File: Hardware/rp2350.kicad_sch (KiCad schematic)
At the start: 40 parts, among them J1 Conn_01x03, J5 USB_C_Receptacle, SW1 SMD_4.6x2.8mm_h2.5mm, SW2 SMD_4.6x2.8mm_h2.5mm, SW4 SMD_4.6x2.8mm_h2.5mm, U4 W25Q128JVPIM

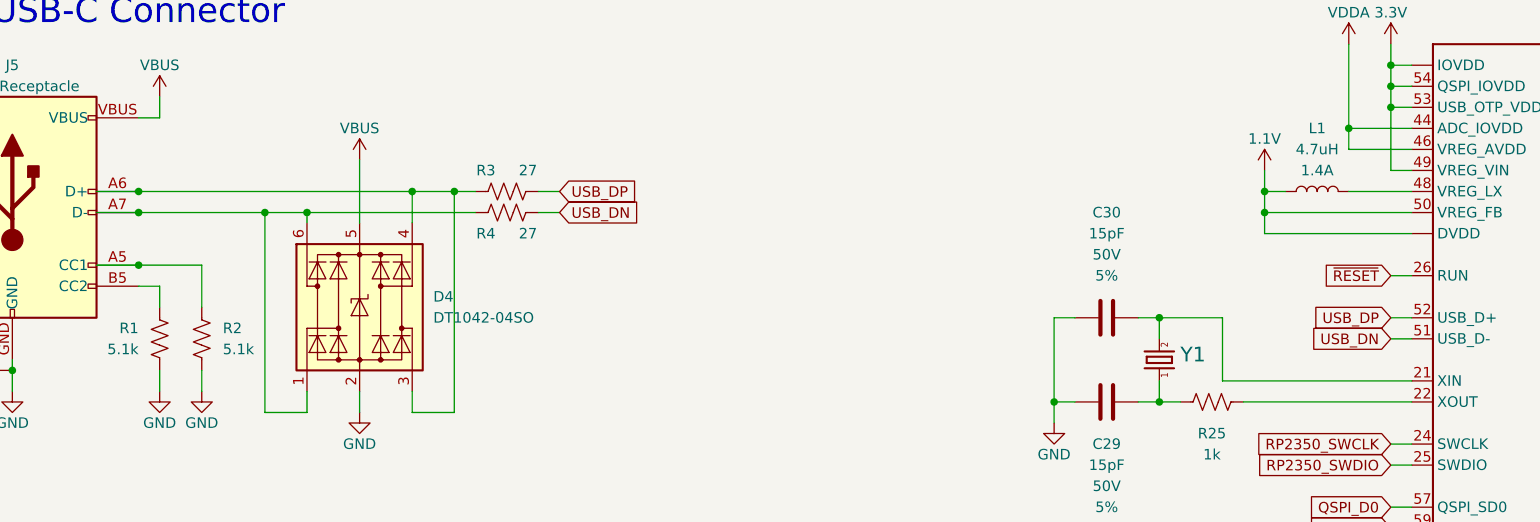
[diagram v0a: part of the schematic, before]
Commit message: Initial board layout
Board outline determined based off selected enclosure
Clusters of components placed and routed
Waiting for feedback before finishing routing
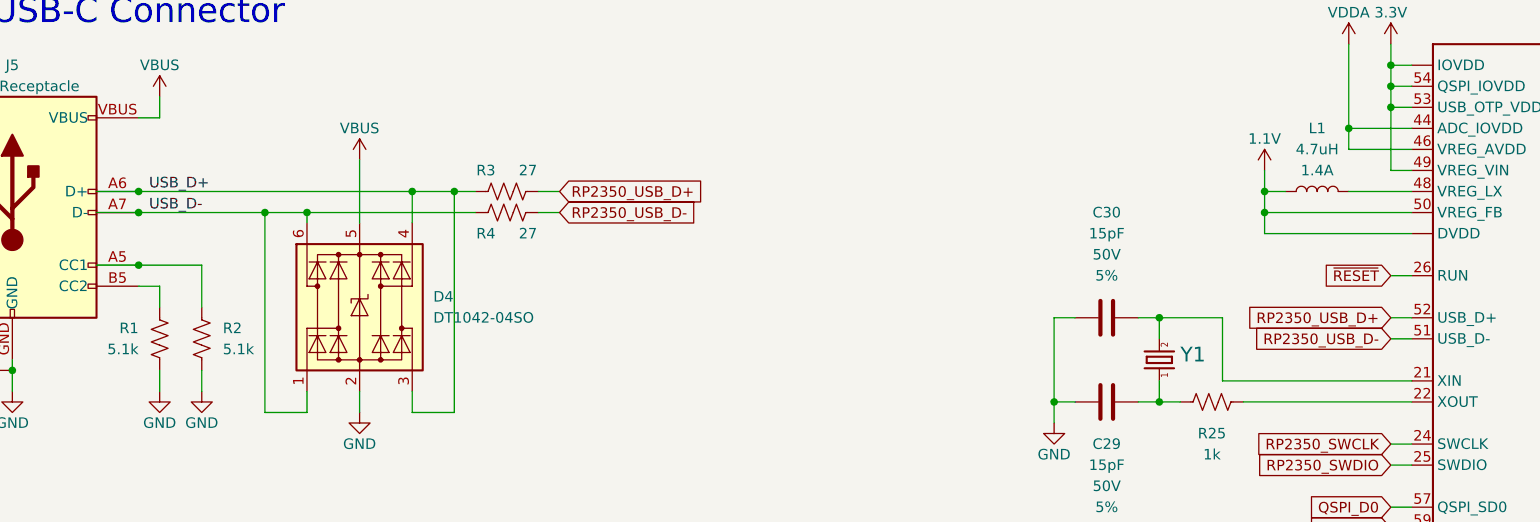
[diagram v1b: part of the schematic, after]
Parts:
- removed SW4: SMD_4.6x2.8mm_h2.5mm, SparkFun-Switch:Push_SMD_4.6x2.8mm, symbol SparkFun-Switch:SPST_Push_SMD_4.6x2.8mm_h2.5mm
- added SW4: PTH_RA_h7.5mm, SparkFun-Switch:Push_PTH_RA_8-020_h7.5mm, symbol SparkFun-Switch:SPST_Push_PTH_RA_h7.5mm
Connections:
- net GND: now also SW4.1
- net USER_BUTTON: now also SW4.2
- net USB_D-: now reaches D4.1 (I/O1), D4.6 (I/O4), J5.A7 (D-), J5.B7 (D-), R4.2
- net USB_D+: now reaches D4.3 (I/O2), D4.4 (I/O3), J5.A6 (D+), J5.B6 (D+), R3.2
- net USB_DN renamed RP2350_USB_D-
- net USB_DP renamed RP2350_USB_D+
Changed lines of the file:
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@@
 		)
 	)
+	(label "USB_D+"
+		(at 58.42 45.72 0)
+		(fields_autoplaced yes)
+		(effects
+			(font
+				(size 1.27 1.27)
+			)
+			(justify left bottom)
+		)
+	)
+	(label "USB_D-"
+		(at 58.42 48.26 0)
+		(fields_autoplaced yes)
+		(effects
+			(font
+				(size 1.27 1.27)
+			)
+			(justify left bottom)
+		)
+	)
 	(global_label "~{BOOT}"
 		(shape input)
@@
 		)
 	)
-	(global_label "USB_DN"
+	(global_label "RP2350_USB_D-"
 		(shape input)
 		(at 107.95 48.26 0)
@@
 		)
 		(property "Intersheetrefs" "${INTERSHEET_REFS}"
-			(at 118.3133 48.26 0)
+			(at 126.9008 48.26 0)
 			(effects
 				(font
@@
 		)
 	)
-	(global_label "USB_DN"
+	(global_label "RP2350_USB_D-"
 		(shape input)
 		(at 208.28 63.5 180)
@@
 		)
 		(property "Intersheetrefs" "${INTERSHEET_REFS}"
-			(at 197.9167 63.5 0)
+			(at 189.3292 63.5 0)
 			(effects
 				(font
@@
 		)
 	)
-	(global_label "USB_DP"
+	(global_label "RP2350_USB_D+"
 		(shape input)
 		(at 208.28 60.96 180)
@@
 		)
 		(property "Intersheetrefs" "${INTERSHEET_REFS}"
-			(at 197.9772 60.96 0)
+			(at 189.3292 60.96 0)
 			(effects
 				(font
@@
 		)
 	)
-	(global_label "USB_DP"
+	(global_label "RP2350_USB_D+"
 		(shape input)
 		(at 107.95 45.72 0)
@@
 		)
 		(property "Intersheetrefs" "${INTERSHEET_REFS}"
-			(at 118.2528 45.72 0)
+			(at 126.9008 45.72 0)
 			(effects
 				(font
@@
 	)
 	(symbol
-		(lib_id "SparkFun-Switch:SPST_Push_SMD_4.6x2.8mm_h2.5mm")
-		(at 35.56 137.16 90)
-		(unit 1)
-		(exclude_from_sim no)
-		(in_bom yes)
-		(on_board yes)
-		(dnp no)
-		(fields_autoplaced yes)
-		(property "Reference" "SW4"
-			(at 36.83 137.1599 90)
-			(effects
-				(font
-					(size 1.27 1.27)
-				)
-				(justify right)
-			)
-		)
-		(property "Value" "SMD_4.6x2.8mm_h2.5mm"
-			(at 36.83 138.4299 90)
-			(effects
-				(font
-					(size 1.27 1.27)
-				)
-				(justify right)
-				(hide yes)
-			)
-		)
-		(property "Footprint" "SparkFun-Switch:Push_SMD_4.6x2.8mm"
-			(at 40.64 137.16 0)
-			(effects
-				(font
-					(size 1.27 1.27)
-				)
-				(hide yes)
-			)
-		)
-		(property "Datasheet" "~"
-			(at 45.72 137.16 0)
-			(effects
-				(font
-					(size 1.27 1.27)
-				)
-				(hide yes)
-			)
-		)
-		(property "Description" "Single Pole Single Throw (SPST) switch"
-			(at 35.56 137.16 0)
-			(effects
-				(font
-					(size 1.27 1.27)
-				)
-				(hide yes)
-			)
-		)
-		(property "PROD_ID" "SWCH-15606"
-			(at 43.18 137.16 0)
-			(effects
-				(font
-					(size 1.27 1.27)
-				)
-				(hide yes)
-			)
-		)
-		(pin "2"
-		)
-		(pin "1"
-		)
-		(instances
-			(project "SparkFun_IoT_Node_LoRaWAN"
-				(path "/e3dd3ae4-244d-4cba-9cca-5d2abf83f29a/590da06b-12fb-4a03-9ce6-308c286b4365"
-					(reference "SW4")
-					(unit 1)
-				)
-			)
-		)
-	)
-	(symbol
 		(lib_id "RP2350A:RP2350A")
 		(at 228.6 68.58 0)
@@
 					(unit 1)
 				)
+			)
+		)
+	)
+	(symbol
+		(lib_id "SparkFun-Switch:SPST_Push_PTH_RA_h7.5mm")
+		(at 35.56 137.16 90)
+		(unit 1)
+		(exclude_from_sim no)
+		(in_bom yes)
+		(on_board yes)
+		(dnp no)
+		(fields_autoplaced yes)
+		(property "Reference" "SW4"
+			(at 36.83 137.1599 90)
+			(effects
+				(font
+					(size 1.27 1.27)
+				)
+				(justify right)
+			)
+		)
+		(property "Value" "PTH_RA_h7.5mm"
+			(at 36.83 138.4299 90)
+			(effects
+				(font
+					(size 1.27 1.27)
+				)
+				(justify right)
+				(hide yes)
+			)
+		)
+		(property "Footprint" "SparkFun-Switch:Push_PTH_RA_8-020_h7.5mm"
+			(at 40.64 137.16 0)
+			(effects
+				(font
+					(size 1.27 1.27)
+				)
+				(hide yes)
+			)
+		)
+		(property "Datasheet" "~"
+			(at 45.72 137.16 0)
+			(effects
+				(font
+					(size 1.27 1.27)
+				)
+				(hide yes)
+			)
+		)
+		(property "Description" "Single Pole Single Throw (SPST) switch"
+			(at 35.56 137.16 0)
+			(effects
+				(font
+					(size 1.27 1.27)
+				)
+				(hide yes)
+			)
+		)
+		(property "PROD_ID" "SWCH-13896"
+			(at 43.18 137.16 0)
+			(effects
+				(font
+					(size 1.27 1.27)
+				)
+				(hide yes)
+			)
+		)
+		(property "Mfg Part#" "8-020 TS H = 7.5mm"
+			(at 48.26 137.16 0)
+			(effects
+				(font
+					(size 1.27 1.27)
+				)
+				(hide yes)
+			)
+		)
+		(pin "M2"
+		)
+		(pin "1"
+		)
+		(pin "M1"
+		)
+		(pin "2"
+		)
+		(instances
+			(project ""
+				(path "/e3dd3ae4-244d-4cba-9cca-5d2abf83f29a/590da06b-12fb-4a03-9ce6-308c286b4365"
+					(reference "SW4")
+					(unit 1)
+				)

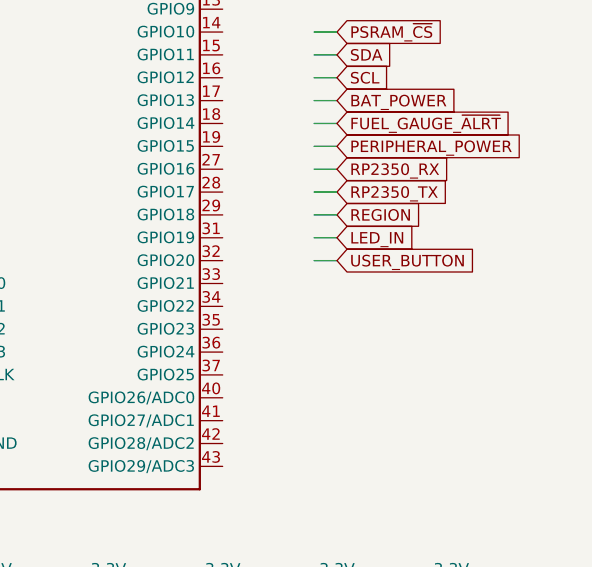
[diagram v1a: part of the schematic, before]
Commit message: Review updates
Remove region selection resistors
Add uSD card connector
Move XBLR USB connector within enclosure
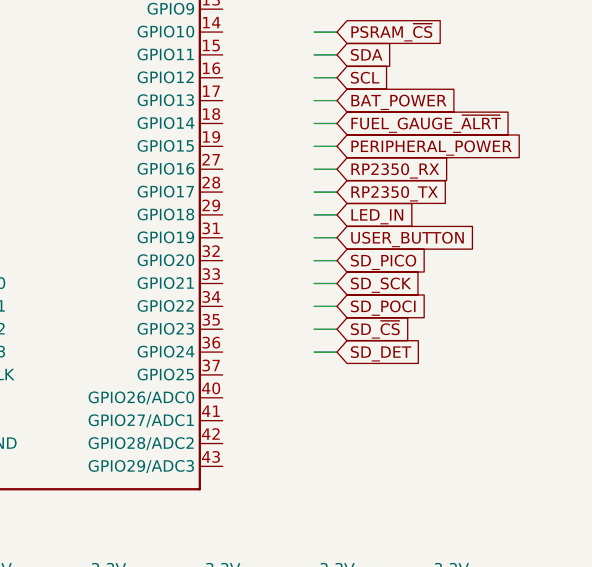
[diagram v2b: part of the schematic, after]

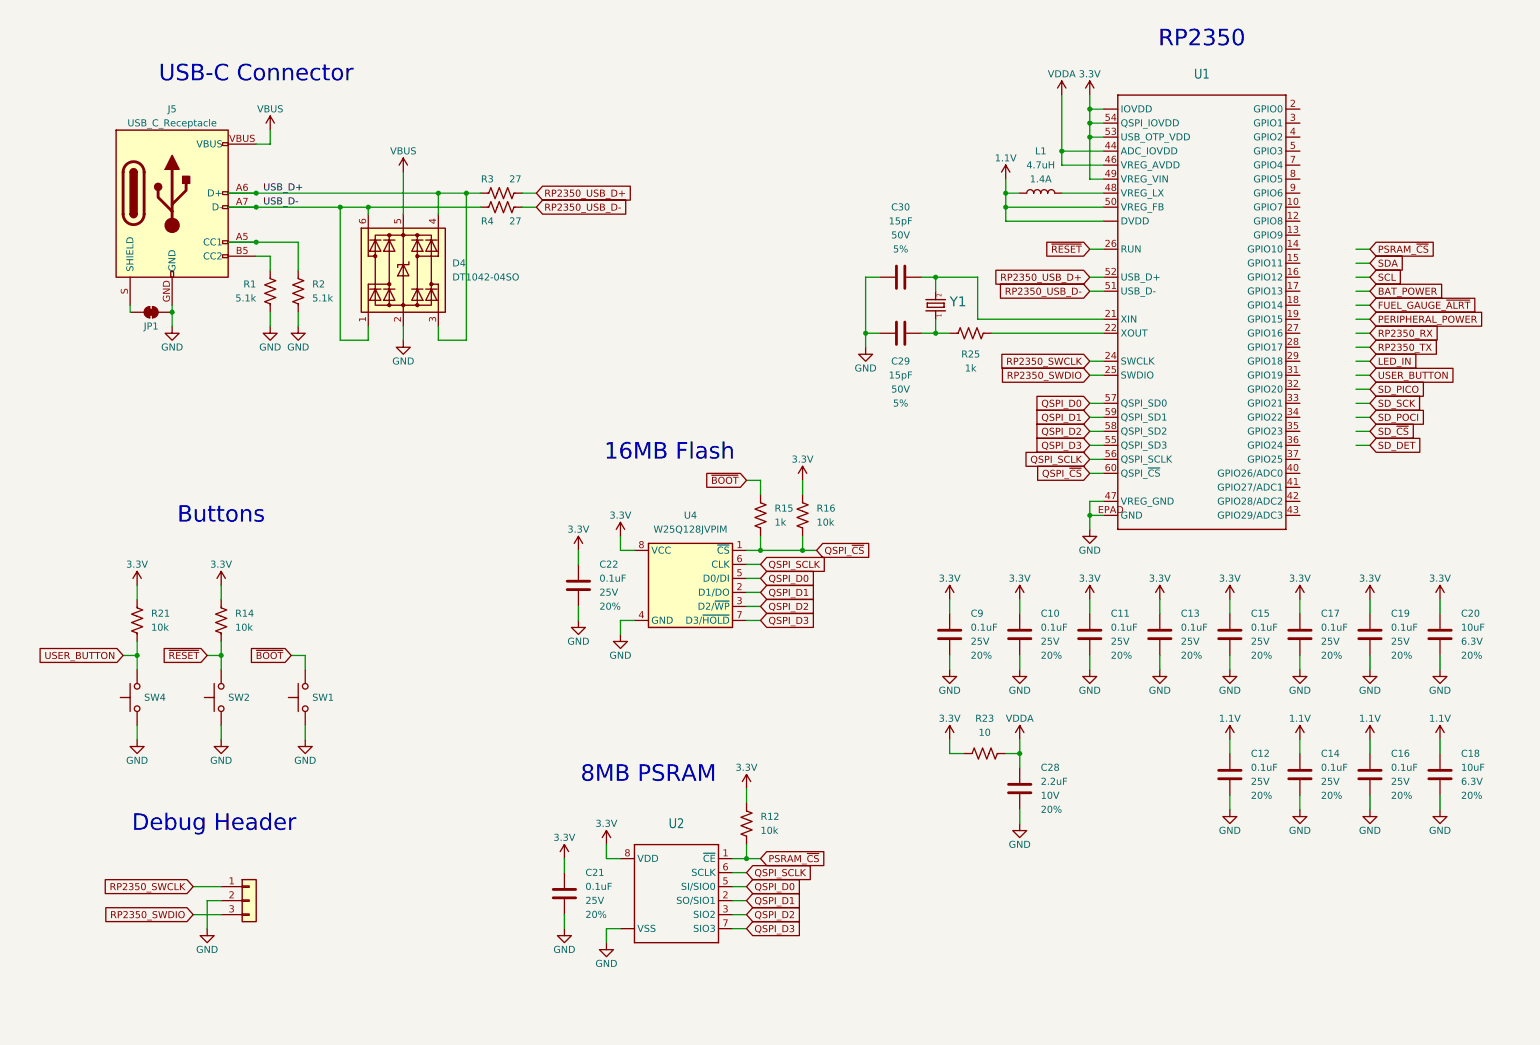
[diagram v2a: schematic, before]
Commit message: Finish connections and routing
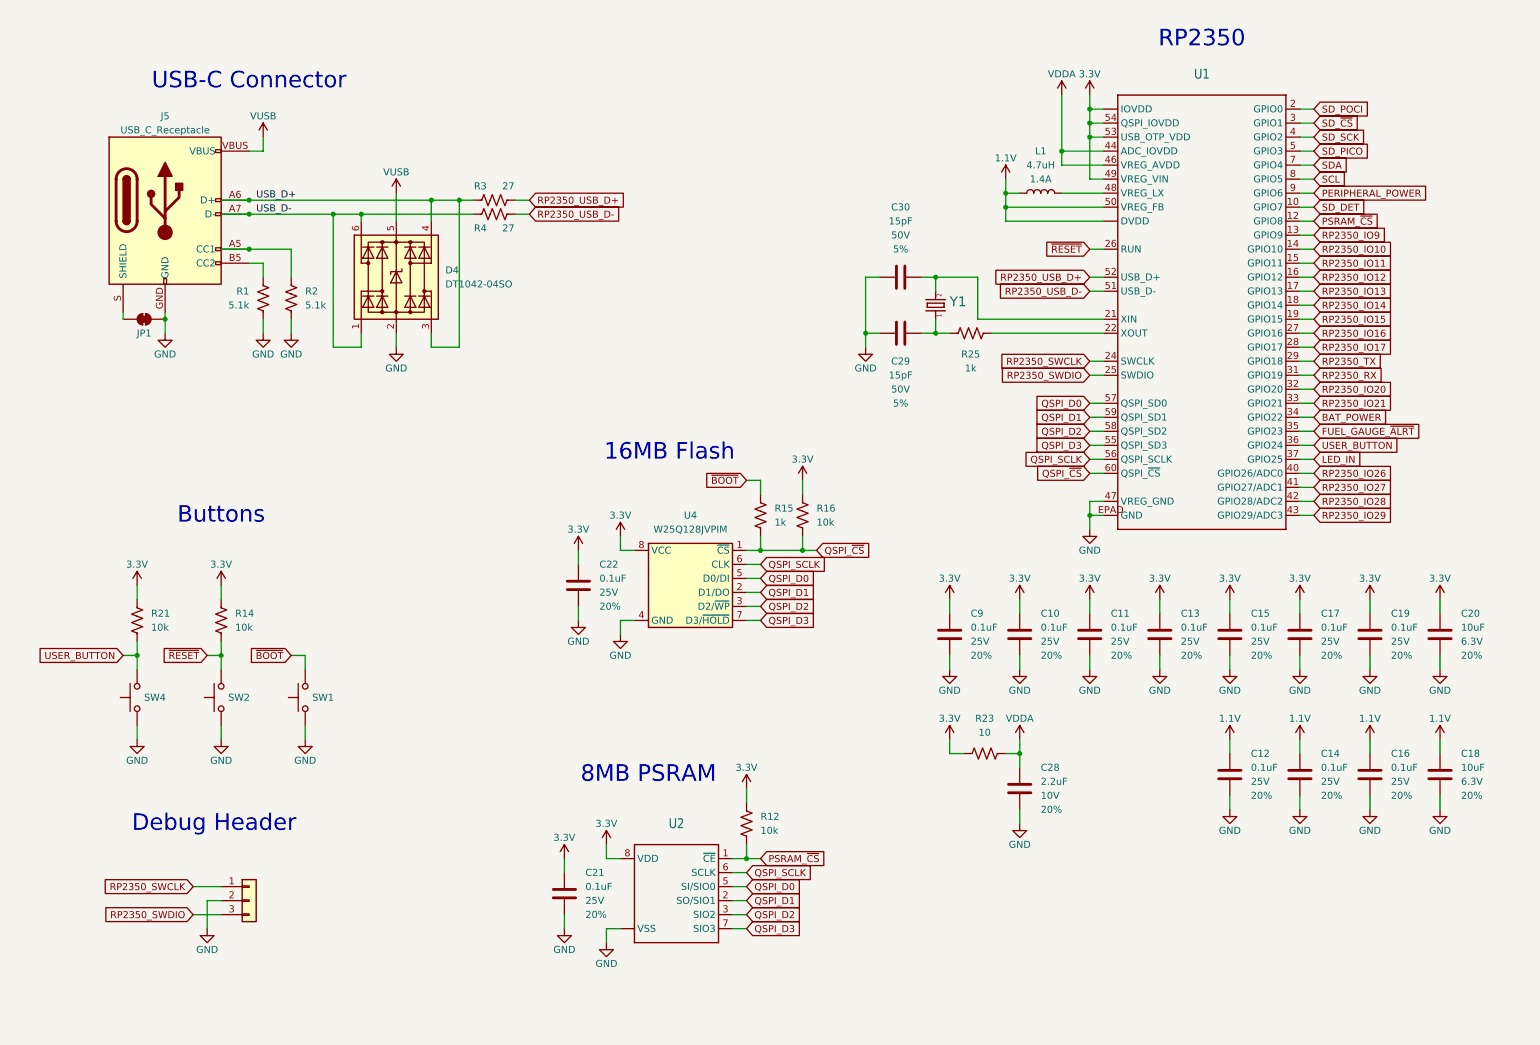
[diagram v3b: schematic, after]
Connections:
- net BAT_POWER: now also U1.34 (GPIO22)
- net FUEL_GAUGE_~{ALRT}: now also U1.35 (GPIO23)
- net LED_IN: now also U1.37 (GPIO25)
- net PERIPHERAL_POWER: now also U1.9 (GPIO6)
- net PSRAM_~{CS}: now also U1.12 (GPIO8)
- net RP2350_RX: now also U1.31 (GPIO19)
- net RP2350_TX: now also U1.29 (GPIO18)
- net SCL: now also U1.8 (GPIO5)
- net SDA: now also U1.7 (GPIO4)
- net SD_DET: now also U1.10 (GPIO7)
- net SD_PICO: now also U1.5 (GPIO3)
- net SD_POCI: now also U1.2 (GPIO0)
- net SD_SCK: now also U1.4 (GPIO2)
- net SD_~{CS}: now also U1.3 (GPIO1)
- net USER_BUTTON: now also U1.36 (GPIO24)
- net RP2350_IO9: now reaches U1.13 (GPIO9)
- net RP2350_IO10: now reaches U1.14 (GPIO10)
- net RP2350_IO11: now reaches U1.15 (GPIO11)
- net RP2350_IO12: now reaches U1.16 (GPIO12)
- net RP2350_IO13: now reaches U1.17 (GPIO13)
- net RP2350_IO14: now reaches U1.18 (GPIO14)
- net RP2350_IO15: now reaches U1.19 (GPIO15)
- net RP2350_IO16: now reaches U1.27 (GPIO16)
- net RP2350_IO17: now reaches U1.28 (GPIO17)
- net RP2350_IO20: now reaches U1.32 (GPIO20)
- net RP2350_IO21: now reaches U1.33 (GPIO21)
- net RP2350_IO26: now reaches U1.40 (GPIO26/ADC0)
- net RP2350_IO27: now reaches U1.41 (GPIO27/ADC1)
- net RP2350_IO28: now reaches U1.42 (GPIO28/ADC2)
- net RP2350_IO29: now reaches U1.43 (GPIO29/ADC3)
- net VBUS renamed VUSB
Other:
- moved on the sheet: D4, J5, JP1, R1, R2, R3, R4

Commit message: Clean up schematic
Add lines between regions
Add instruction text to all jumpers
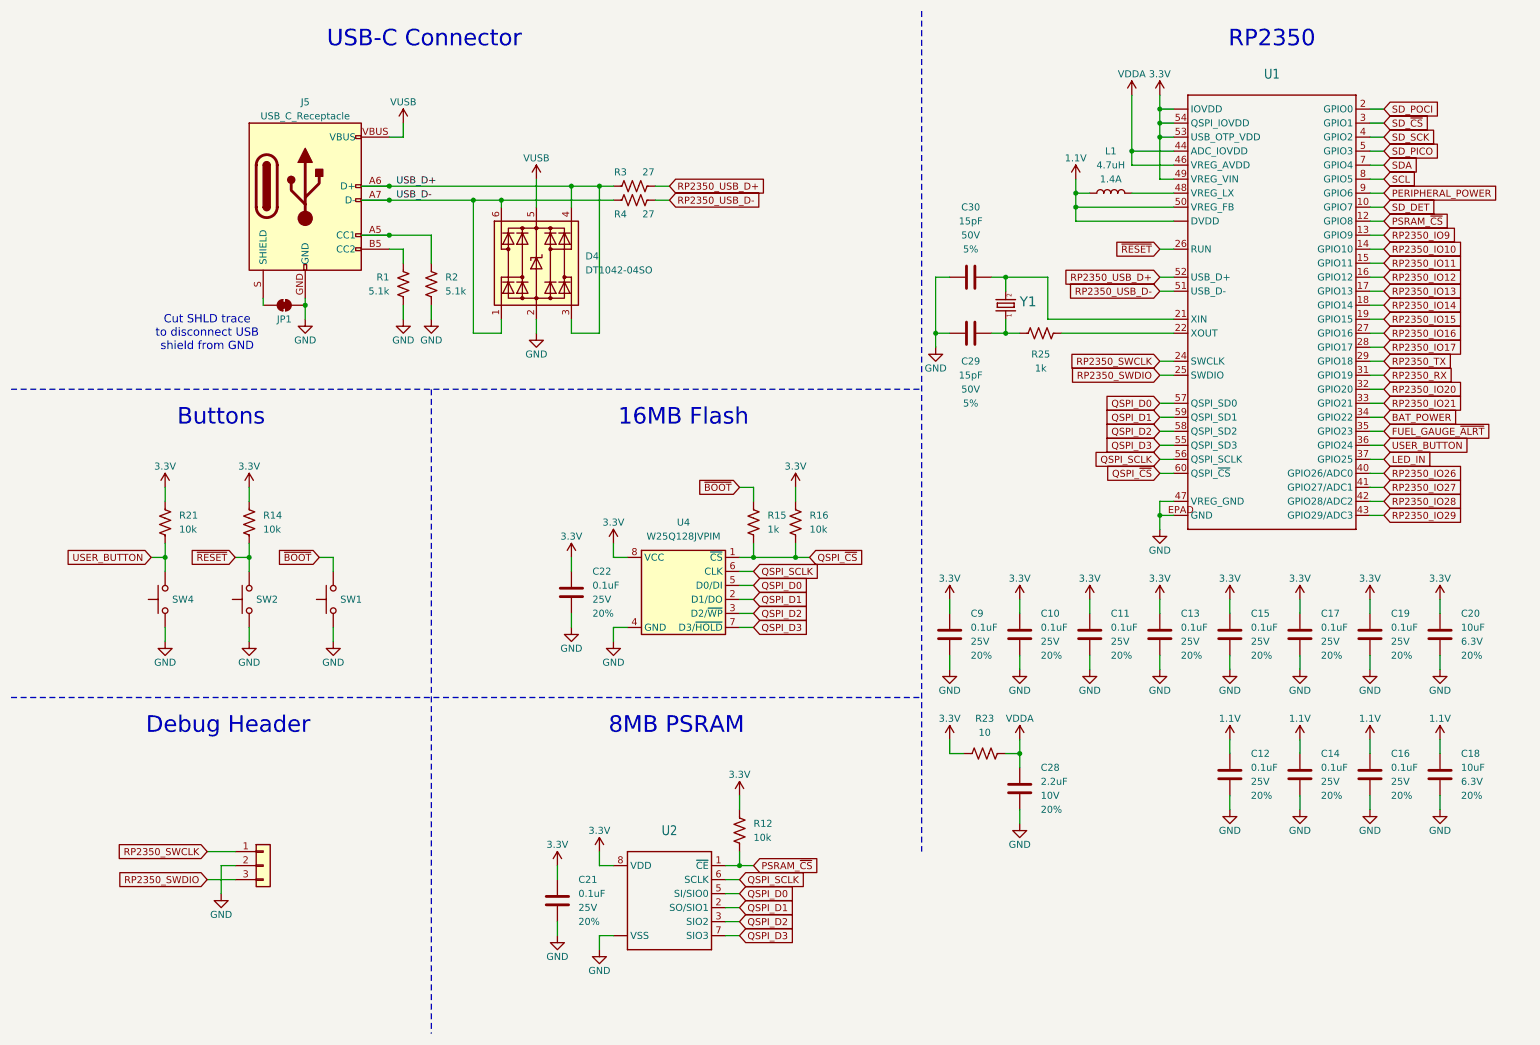
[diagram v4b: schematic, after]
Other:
- note added: "Cut SHLD trace to disconnect USB shield from GND"
- moved on the sheet: C21, C22, C29, C30, D4, J5, JP1, L1, R1, R12, R14, R15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
